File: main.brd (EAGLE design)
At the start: 22 x 112 mm, 51 parts, among them Q1 2N2222, Q2 2N2222, Q3 2N2222, Q4 N_MOSFET_DEVSOT23-6L_PKG, U1 MAX_485_DEV3D, U2 BQ24072TRGTR_DEVBQ24072TRGTR, U3 LD1117S33CTR_DEVLD1117S33CTR, U4 ESP_32_WROVER_I_PKG, U5 USB_TO_UART_DEV, U6 AP9214L_DEV, X1 XLR_FEMALE_PLUG_DEV, X2 USB_ALI_DEV

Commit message: V1_1
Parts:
- moved B1 0.25 mm to (10.8, 39.0)
- moved C1 0.25 mm to (8.75, 90.0)
- moved C10 0.25 mm to (10.2, 15.7)
- moved C11 0.25 mm to (13.2, 15.7)
- moved C12 0.25 mm to (11.8, 15.7)
- moved C13 0.25 mm to (15.8, 12.0)
- moved C14 0.25 mm to (14.2, 11.9)
- moved C15 0.25 mm to (17.8, 3.00)
- moved C16 0.25 mm to (8.50, 69.4)
- moved C2 0.25 mm to (7.25, 90.0)
- moved C3 0.25 mm to (10.8, 77.0)
- moved C4 0.25 mm to (14.8, 71.0)
- moved C5 0.25 mm to (7.75, 63.3)
- moved C6 0.25 mm to (2.25, 58.0)
- moved C7 0.25 mm to (2.25, 56.5)
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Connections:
- net GND: now also U2.GP1, U2.GP2, U2.GP3, U2.GP4, U4.GP1, U4.GP2, U4.GP3, U4.GP4, U4.GP5, U4.GP6, U4.GP8, U4.GP9, U5.GP1, U5.GP2, U5.GP3, U5.GP4; no longer U2.17, U4.P$39, U5.GND
- net PROTECTION_THERMAL_PAD: now also U6.EP1, U6.EP2, U6.EP3, U6.EP4; no longer U6.EP
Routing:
- net GND: track 19.5 -> 32.3 mm, vias 366 -> 333
- net PROTECTION_THERMAL_PAD: track 2.83 -> 0.42 mm, vias 9 -> 4
- net 3.3V: track 27.3 -> 27.1 mm, vias 11 -> 12
- added copper zone on layer 1, net REDRUM
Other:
- board size 22 x 112 mm -> 21.5 x 112 mm
- board text added: "V1.1"
- board text removed: "V1.0"

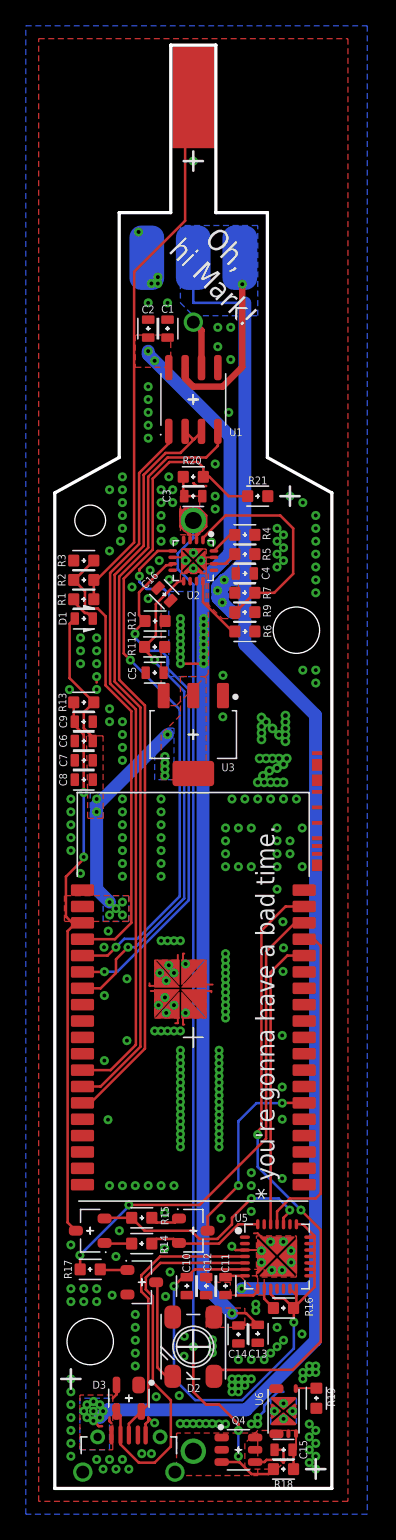
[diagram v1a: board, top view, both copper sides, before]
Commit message: fixed tab problems plus made some simplifications
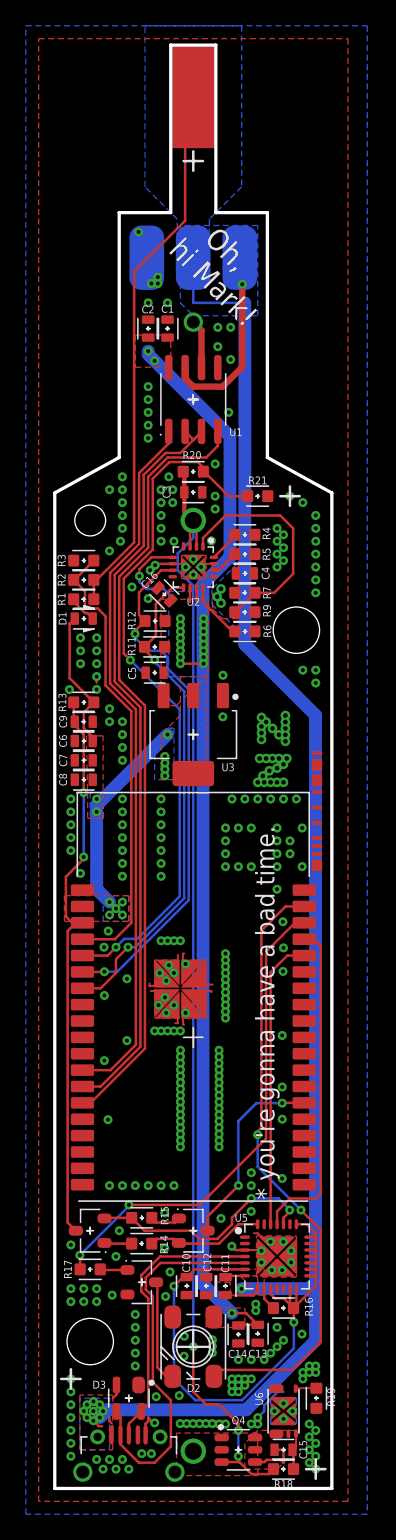
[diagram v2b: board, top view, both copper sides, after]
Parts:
- moved U2 0.50 mm to (10.8, 71.5)
- moved R20 0.40 mm to (10.8, 78.9)
- moved C3 0.30 mm to (10.8, 77.3)
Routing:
- net 5V: track 132.5 -> 122.1 mm
- net VBAT: track 95.2 -> 89.1 mm
- net 4.2V: track 92.1 -> 94.1 mm
- net VDD_USB: track 44.1 -> 45.5 mm
- net TS: track 17.6 -> 18.1 mm
- net N$34: track 5.03 -> 4.53 mm
- net GND: track 32.3 -> 32.6 mm, vias 333 -> 331
- removed copper zone on layer 1, net VBAT
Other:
- board text added: "V1.3"
- board text removed: "V1.1"

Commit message: made the aperature size a bit bigger .3 -> .34
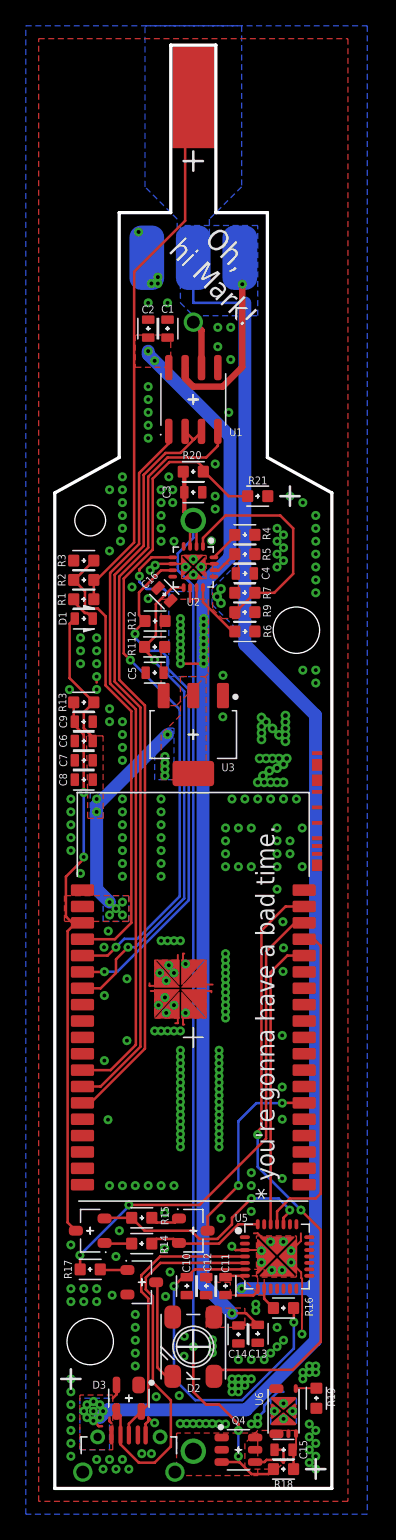
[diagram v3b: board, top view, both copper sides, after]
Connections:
- new net N$41: U5.10
- new net N$42: U5.14
- new net N$43: U5.13
- new net N$44: U5.15
- new net N$45: U5.16
- new net N$46: U5.17
- new net N$47: U5.18
- new net N$48: U5.19
- new net N$49: U5.20
- new net N$50: U5.21
- new net N$51: U5.22
- net VDD_USB: no longer U5.10, U5.13, U5.14, U5.15, U5.16, U5.17, U5.18, U5.19, U5.20, U5.21, U5.22
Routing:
- net VDD_USB: track 45.5 -> 28.3 mm
- net GND: track 32.6 -> 40.2 mm
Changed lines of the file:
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@@
 <layer number="27" name="tValues" color="7" fill="1" visible="yes" active="yes"/>
 <layer number="28" name="bValues" color="7" fill="1" visible="yes" active="yes"/>
-<layer number="29" name="tStop" color="7" fill="3" visible="yes" active="yes"/>
+<layer number="29" name="tStop" color="7" fill="3" visible="no" active="yes"/>
 <layer number="30" name="bStop" color="7" fill="6" visible="yes" active="yes"/>
 <layer number="31" name="tCream" color="63" fill="1" visible="yes" active="yes"/>
@@
 <attribute name="PN" value="MAX485EESA+TCT-ND " x="10.75" y="84.5" size="1.778" layer="27" rot="R90" display="off"/>
 </element>
-<element name="U5" library="Blizzard_Library" library_urn="urn:adsk.eagle:library:2665040" package="QFN50P500X500X100-28" package3d_urn="urn:adsk.eagle:package:2665053/5" value="USB_TO_UART_DEV" x="17.25" y="18" smashed="yes">
+<element name="U5" library="Blizzard_Library" library_urn="urn:adsk.eagle:library:2665040" package="QFN50P500X500X100-28" package3d_urn="urn:adsk.eagle:package:2665053/7" value="USB_TO_UART_DEV" x="17.25" y="18" smashed="yes">
 <attribute name="NAME" x="14.474" y="21.3091" size="0.6096" layer="25" rot="R180" align="bottom-center"/>
 <attribute name="PN" value="CP2102" x="17.25" y="18" size="1.778" layer="27" display="off"/>
@@
 <attribute name="NAME" x="14.19" y="10.7514" size="0.6096" layer="25" rot="R180" align="bottom-center"/>
 </element>
-<element name="U2" library="Blizzard_Library" library_urn="urn:adsk.eagle:library:2665040" package="QFN50P300X300X100-17T168" package3d_urn="urn:adsk.eagle:package:7249956/6" value="BQ24072TRGTR_DEVBQ24072TRGTR" x="10.75" y="71.5" smashed="yes" rot="R270">
+<element name="U2" library="Blizzard_Library" library_urn="urn:adsk.eagle:library:2665040" package="QFN50P300X300X100-17T168" package3d_urn="urn:adsk.eagle:package:7249956/7" value="BQ24072TRGTR_DEVBQ24072TRGTR" x="10.75" y="71.5" smashed="yes" rot="R270">
 <attribute name="NAME" x="10.75" y="68.5" size="0.6096" layer="25" align="bottom-center"/>
 <attribute name="PN" value="BQ24072TRGTR" x="10.75" y="71.5" size="1.778" layer="27" rot="R270" display="off"/>
@@
 <wire x1="9.15" y1="71.75" x2="7.899" y2="71.75" width="0.2" layer="1"/>
 <wire x1="7.899" y1="71.75" x2="7.79" y2="71.641" width="0.2" layer="1"/>
+<wire x1="19.18" y1="11.98" x2="19.18" y2="13.49129375" width="0.1524" layer="1"/>
+<wire x1="19.18" y1="13.49129375" x2="19.19315" y2="13.50444375" width="0.1524" layer="1"/>
+<wire x1="19.1214" y1="16.7586" x2="18.34" y2="17.54" width="0.1524" layer="1"/>
+<wire x1="19.1214" y1="16.34318125" x2="19.1214" y2="16.7586" width="0.1524" layer="1"/>
+<wire x1="19.19315" y1="13.50444375" x2="19.19315" y2="16.27143125" width="0.1524" layer="1"/>
+<wire x1="19.19315" y1="16.27143125" x2="19.1214" y2="16.34318125" width="0.1524" layer="1"/>
+<wire x1="18.34" y1="18.44" x2="19.1" y2="19.2" width="0.1524" layer="1"/>
+<wire x1="19.1" y1="19.2" x2="19.1" y2="19.8" width="0.1524" layer="1"/>
 <wire x1="10.75" y1="72.1" x2="10.75" y2="72.2" width="0" layer="19" extent="1-1"/>
 <wire x1="11.45" y1="71.5" x2="11.35" y2="71.5" width="0" layer="19" extent="1-1"/>
@@
 <contactref element="U5" pad="6"/>
 <contactref element="C10" pad="2"/>
-<contactref element="U5" pad="22"/>
-<contactref element="U5" pad="21"/>
-<contactref element="U5" pad="20"/>
-<contactref element="U5" pad="19"/>
-<contactref element="U5" pad="18"/>
-<contactref element="U5" pad="17"/>
-<contactref element="U5" pad="16"/>
-<contactref element="U5" pad="15"/>
-<contactref element="U5" pad="13"/>
 <contactref element="R16" pad="1"/>
-<contactref element="U5" pad="10"/>
-<contactref element="U5" pad="14"/>
-<wire x1="18.25" y1="14.1287" x2="18.3787" y2="14" width="0.2" layer="1"/>
 <wire x1="18.75" y1="14.2203" x2="18.5297" y2="14" width="0.2" layer="1"/>
-<wire x1="18.5297" y1="14" x2="20.25" y2="15.7203" width="0.2" layer="1"/>
-<wire x1="20.25" y1="15.7203" x2="20.25" y2="16.5" width="0.2" layer="1"/>
-<wire x1="20.25" y1="16.5" x2="20.25" y2="17.5" width="0.2" layer="1"/>
-<wire x1="20.25" y1="17.5" x2="20.25" y2="18" width="0.2" layer="1"/>
-<wire x1="20.25" y1="18" x2="20.25" y2="18.5" width="0.2" layer="1"/>
-<wire x1="20.25" y1="18.5" x2="20.25" y2="19" width="0.2" layer="1"/>
-<wire x1="20.25" y1="19" x2="20.25" y2="19.5" width="0.2" layer="1"/>
-<wire x1="20.25" y1="19.8" x2="20.25" y2="19.5" width="0.2" layer="1"/>
 <via x="18.55" y="12.9" extent="1-16" drill="0.3"/>
 <wire x1="18.5297" y1="14" x2="18.55" y2="13.9797" width="0.2" layer="1"/>
@@
 <wire x1="9.25" y1="8.5" x2="10.8976" y2="6.8524" width="0.2" layer="16"/>
 <wire x1="10.8976" y1="6.8524" x2="14.53834375" y2="6.8524" width="0.2" layer="16"/>
-<wire x1="19.75" y1="16.5" x2="20.25" y2="16.5" width="0.2" layer="1"/>
-<wire x1="19.75" y1="17" x2="20.1" y2="17" width="0.2" layer="1"/>
-<wire x1="19.75" y1="18" x2="20.25" y2="18" width="0.2" layer="1"/>
-<wire x1="19.75" y1="18.5" x2="20.25" y2="18.5" width="0.2" layer="1"/>
-<wire x1="19.75" y1="19" x2="20.25" y2="19" width="0.2" layer="1"/>
-<wire x1="19.75" y1="19.5" x2="20.25" y2="19.5" width="0.2" layer="1"/>
 <wire x1="9.25" y1="15.7" x2="9.9463" y2="16.3963" width="0.2" layer="1"/>
 <wire x1="9.9463" y1="16.3963" x2="10.25" y2="16.3963" width="0.2" layer="1"/>
-<wire x1="18.75" y1="20.5" x2="19.55" y2="20.5" width="0.2" layer="1"/>
-<wire x1="19.55" y1="20.5" x2="20.25" y2="19.8" width="0.2" layer="1"/>
-<wire x1="17.7821" y1="14.7476" x2="18.5297" y2="14" width="0.2" layer="1"/>
-<wire x1="17.08953125" y1="14.7476" x2="17.7821" y2="14.7476" width="0.2" layer="1"/>
-<wire x1="17.08953125" y1="14.7476" x2="16.75" y2="15.08713125" width="0.2" layer="1"/>
-<wire x1="16.75" y1="15.08713125" x2="16.75" y2="15.5" width="0.2" layer="1"/>
-<wire x1="18.75" y1="15.5" x2="18.75" y2="14.2203" width="0.2" layer="1"/>
 <wire x1="14.75" y1="17" x2="10.8537" y2="17" width="0.2" layer="1"/>
 <wire x1="10.8537" y1="17" x2="10.25" y2="16.3963" width="0.2" layer="1"/>
-<wire x1="18.25" y1="15.5" x2="18.25" y2="14.1287" width="0.2" layer="1"/>
-<wire x1="19.75" y1="17.5" x2="20.25" y2="17.5" width="0.2" layer="1"/>
-<wire x1="19.75" y1="17.5" x2="19.75" y2="17" width="0" layer="19" extent="1-1"/>
-<wire x1="18.3787" y1="14" x2="18.5297" y2="14" width="0" layer="19" extent="1-1"/>
 </signal>
 <signal name="D-">
@@
 </polygon>
 </signal>
+<signal name="N$41">
+<contactref element="U5" pad="10"/>
+</signal>
+<signal name="N$42">
+<contactref element="U5" pad="14"/>
+</signal>
+<signal name="N$43">
+<contactref element="U5" pad="13"/>
+</signal>
+<signal name="N$44">
+<contactref element="U5" pad="15"/>
+</signal>
+<signal name="N$45">
+<contactref element="U5" pad="16"/>
+</signal>
+<signal name="N$46">
+<contactref element="U5" pad="17"/>
+</signal>
+<signal name="N$47">
+<contactref element="U5" pad="18"/>
+</signal>
+<signal name="N$48">
+<contactref element="U5" pad="19"/>
+</signal>
+<signal name="N$49">
+<contactref element="U5" pad="20"/>
+</signal>
+<signal name="N$50">
+<contactref element="U5" pad="21"/>
+</signal>
+<signal name="N$51">
+<contactref element="U5" pad="22"/>
+</signal>
 </signals>

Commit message: v1.5
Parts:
- moved U2 0.05 mm to (10.7, 71.5)
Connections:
- net 4.2V: no longer U2.11
- net VBAT: no longer U2.3
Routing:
- net GND: track 40.2 -> 36.3 mm, vias 331 -> 330
- net VBAT: track 89.1 -> 87.1 mm
- net N$37: track 2.42 -> 2.94 mm
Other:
- board text added: "V1.5"
- board text removed: "V1.3"

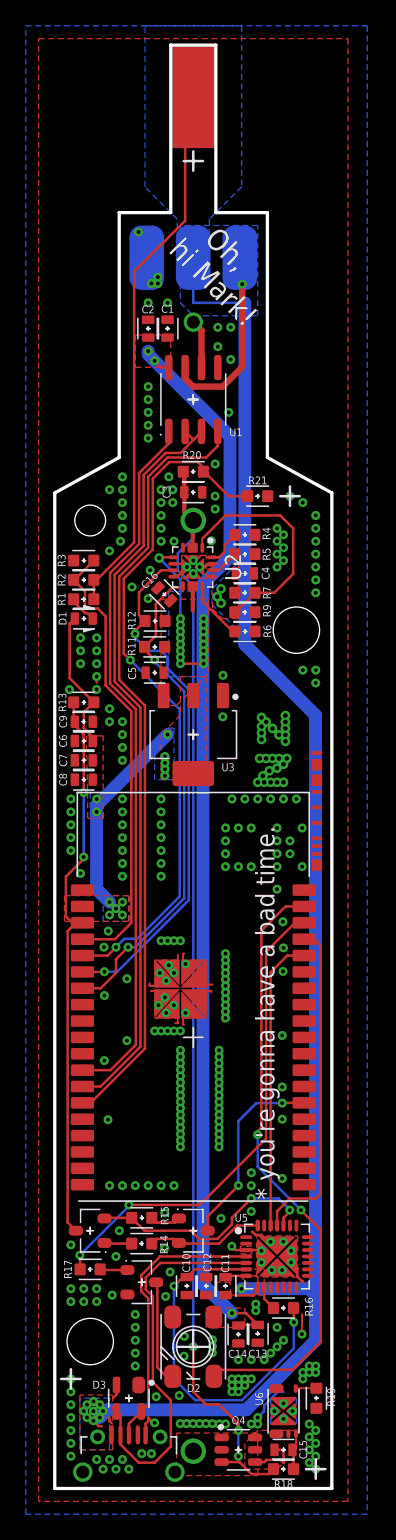
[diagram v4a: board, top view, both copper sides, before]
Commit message: redacted battery saftey chips
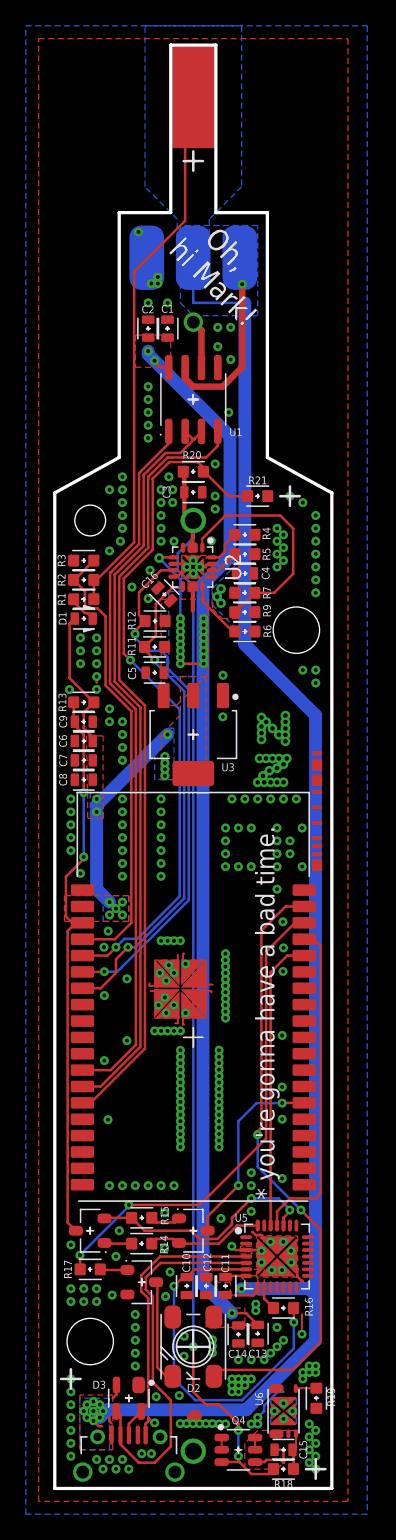
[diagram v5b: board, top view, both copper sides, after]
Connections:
- net BATTERY_GROUND: no longer B1.-
- net GND: now also B1.-
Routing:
- net BATTERY_GROUND: track 0.00 -> 1.90 mm
- removed copper zone on layer 1, net BATTERY_GROUND
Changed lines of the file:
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@@
 <?xml version="1.0" encoding="utf-8"?>
 <!DOCTYPE eagle SYSTEM "eagle.dtd">
-<eagle version="9.5.2">
+<eagle version="9.6.1">
 <drawing>
 <settings>
@@
 </layers>
 <board>
-<fusionsync huburn="a.cGVyc29uYWw6dWUyYTJlM2Uz" projecturn="a.cGVyc29uYWw6dWUyYTJlM2UzIzIwMTgwNDEyMTI3MjgyNzA2" f3durn="urn:adsk.wipprod:dm.lineage:-doiME8GTo-qmdWeToWRKw" pcbguid="11756f07-90eb-4fb1-b554-1974a187bae5" lastpulledtime="2019-06-18T15:06:02Z" lastsyncedchangeguid="351d837d-5a63-8e38-a033-b0925656dba5"/>
+<fusionsync huburn="a.cGVyc29uYWw6dWUyYTJlM2Uz" projecturn="a.cGVyc29uYWw6dWUyYTJlM2UzIzIwMTgwNDEyMTI3MjgyNzA2" f3durn="urn:adsk.wipprod:dm.lineage:-doiME8GTo-qmdWeToWRKw" pcbguid="11756f07-90eb-4fb1-b554-1974a187bae5" lastpulledtime="2019-06-18T15:06:02Z" lastsyncedchangeguid="351d837d-5a63-8e38-a033-b0925656dba5" latestrevisionid="" lastsyncedrevisionid="" lastboardhashguid="" lastpushedtime="" linktopcb3d="%12"/>
 <plain>
 <wire x1="4.75" y1="98.5" x2="4.75" y2="122.5" width="0.254" layer="47"/>
@@
 <attribute name="VALUE" x="17.1886" y="12" size="1.27" layer="27" rot="R90" align="top-center"/>
 </element>
-<element name="U2" library="Blizzard_Library" library_urn="urn:adsk.eagle:library:2665040" package="QFN50P300X300X100-17T168" package3d_urn="urn:adsk.eagle:package:7249956/11" value="BQ24072TRGTR_DEVBQ24072TRGTR" x="10.7" y="71.5" smashed="yes" rot="R270">
+<element name="U2" library="Blizzard_Library" library_urn="urn:adsk.eagle:library:2665040" package="QFN50P300X300X100-17T168" package3d_urn="urn:adsk.eagle:package:7249956/12" value="BQ24072TRGTR_DEVBQ24072TRGTR" x="10.7" y="71.5" smashed="yes" rot="R270">
 <attribute name="NAME" x="13.1996" y="71.5" size="1.27" layer="25" rot="R270" align="bottom-center"/>
 <attribute name="PN" value="BQ24072TRGTR" x="10.7" y="71.5" size="1.778" layer="27" rot="R270" display="off"/>
@@
 <wire x1="9.8524" y1="71.08331875" x2="9.8524" y2="71.1524" width="0.2" layer="1"/>
 <wire x1="9.8524" y1="71.1524" x2="10.2" y2="71.5" width="0.2" layer="1"/>
+<contactref element="B1" pad="-"/>
+<wire x1="10.75" y1="5.45" x2="10.9" y2="5.6" width="1.016" layer="1"/>
 <wire x1="10.75" y1="72" x2="10.7" y2="72" width="0" layer="19" extent="1-1"/>
 <wire x1="11.2" y1="71.5" x2="11.25" y2="71.5" width="0" layer="19" extent="1-1"/>
@@
 <contactref element="Q4" pad="1"/>
 <contactref element="Q4" pad="6"/>
-<contactref element="B1" pad="-"/>
 <contactref element="Q4" pad="5"/>
-<polygon width="0.2" layer="1">
-<vertex x="9.45" y="1"/>
-<vertex x="15.75" y="1"/>
-<vertex x="15.75" y="4.3"/>
-<vertex x="9.45" y="4.3"/>
-</polygon>
+<wire x1="15.5472" y1="3.95" x2="15.5472" y2="3" width="0.1524" layer="1"/>
+<wire x1="12.9528" y1="3.95" x2="12.9528" y2="3" width="0.1524" layer="1"/>
+<wire x1="12.9528" y1="3.95" x2="15.5472" y2="3.95" width="0" layer="19" extent="1-1"/>
 </signal>
 <signal name="N$11">
